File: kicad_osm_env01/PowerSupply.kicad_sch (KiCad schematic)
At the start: 79 parts

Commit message: added stml433 to schematic and carried out some mods
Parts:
- removed D1: (no value), symbol device:D_Schottky
- added R?: 1M, Resistor_SMD:R_0603_1608Metric, symbol OSM_env01-rescue:R-ESP32-EVB_Rev_D
- BAT1: value (none) -> 18650; footprint (none) -> Devtank_PCB_lib:BatteryHolder_Keystone_1042_1x18650
- C10: value (none) -> 4.7nF; footprint (none) -> Capacitor_SMD:C_0402_1005Metric
- C11, C3, C4, C9: value (none) -> 47uF; footprint (none) -> Capacitor_SMD:C_0805_2012Metric
- C14, C25, C63, C8: value (none) -> 1uF; footprint (none) -> Capacitor_SMD:C_0402_1005Metric
- C2, C24, C5: value (none) -> 10uF; footprint (none) -> Capacitor_SMD:C_0603_1608Metric
- C22, C23: value (none) -> 100nF; footprint (none) -> Capacitor_SMD:C_0402_1005Metric
- C31, C6, C7: value (none) -> DNF; footprint (none) -> Capacitor_SMD:C_0603_1608Metric
- C32, C72: value (none) -> DNF; footprint (none) -> Capacitor_SMD:C_0402_1005Metric
- C46: value (none) -> DNF; footprint (none) -> Capacitor_SMD:CP_Elec_4x5.4
- D10: value (none) -> DNF; footprint (none) -> Diode_SMD:D_SOD-123
- D11, D15: value (none) -> RED; footprint (none) -> LED_SMD:LED_0603_1608Metric
- D13: value (none) -> GRN; footprint (none) -> Devtank_PCB_lib:LED_Rectangular_W4.5mm_H7.3mm_Horizontal_2.54mm_Z3.0mm
- D14: value (none) -> YLW; footprint (none) -> Devtank_PCB_lib:LED_Rectangular_W4.5mm_H7.3mm_Horizontal_2.54mm_Z3.0mm
- D2, D3, D4, D9: value (none) -> RB160M-40TR; footprint (none) -> Diode_SMD:D_SOD-123
- D5: value (none) -> SMFE5-0A; footprint (none) -> Diode_SMD:D_SOD-123
- L1: value (none) -> 10uH; footprint (none) -> Inductor_SMD:L_1812_4532Metric
- Q1: value (none) -> SI2301BDS-T1-E3; footprint (none) -> Package_TO_SOT_SMD:SOT-23
- Q4: value (none) -> IRF7509TRPBF; footprint (none) -> Package_SO:SO-8_3.9x4.9mm_P1.27mm
- R127, R27, R54: value (none) -> DNF; footprint (none) -> Resistor_SMD:R_0603_1608Metric
- R128, R20, R28, R32, R52: value (none) -> 0R; footprint (none) -> Resistor_SMD:R_0603_1608Metric
- R18, R21, R58: value (none) -> 1M; footprint (none) -> Resistor_SMD:R_0603_1608Metric
- R19, R22, R64: value (none) -> 470k; footprint (none) -> Resistor_SMD:R_0603_1608Metric
- R41, R53: value (none) -> 2.2k; footprint (none) -> Resistor_SMD:R_0603_1608Metric
- R42, R44: value (none) -> 1.6k; footprint (none) -> Resistor_SMD:R_0603_1608Metric
- R43, R45: value (none) -> 4.99k; footprint (none) -> Resistor_SMD:R_0603_1608Metric
- R46: value (none) -> 110k; footprint (none) -> Resistor_SMD:R_0603_1608Metric
- R47: value (none) -> 36k; footprint (none) -> Resistor_SMD:R_0603_1608Metric
- R56: value (none) -> 10k; footprint (none) -> Resistor_SMD:R_0603_1608Metric
- R57, R68, R69: value (none) -> 100k; footprint (none) -> Resistor_SMD:R_0603_1608Metric
- R59, R60, R61, R62: value (none) -> 0R; footprint (none) -> Resistor_SMD:R_0805_2012Metric
- R67: value (none) -> 300k; footprint (none) -> Resistor_SMD:R_0603_1608Metric
- SW3: value (none) -> SW_Push; footprint (none) -> Devtank_PCB_lib:SW_Tactile_SPST_Angled_PTS645Vx58-2LFS
- TH2: value (none) -> 10K; footprint (none) -> Resistor_SMD:R_1206_3216Metric
- TP18, TP27, TP29, TP79: value (none) -> Test_Point; footprint (none) -> TestPoint:TestPoint_Pad_D1.5mm
- TP19, TP26: renamed from TP?; value (none) -> Test_Point; footprint (none) -> TestPoint:TestPoint_THTPad_D1.0mm_Drill0.5mm
- TP25: value (none) -> Test_Point; footprint (none) -> TestPoint:TestPoint_THTPad_D1.0mm_Drill0.5mm
- TP28: renamed from TP?; value (none) -> Test_Point; footprint (none) -> TestPoint:TestPoint_Pad_D1.5mm
- U1: value (none) -> MIC2250-1YD5; footprint (none) -> Package_TO_SOT_SMD:SOT-23-5
- U2: value (none) -> MCP73833; footprint (none) -> Package_SO:MSOP-10_3x3mm_P0.5mm
- U4: value (none) -> MIC5219-3.3; footprint (none) -> Package_TO_SOT_SMD:SOT-23-5
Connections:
- net 5Vin: now also C3.1, C4.1, D11.2 (A), D13.2 (A), D14.2 (A), D15.2 (A), D3.2 (A), D5.1 (A1), Q1.1 (G), U2.1 (VDD1), U2.2 (VDD2)
- net BAT_OP: now also R?.2
- net GND: now also R?.1
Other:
- moved on the sheet: TP79

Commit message: updated mod list
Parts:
- added Q?: 2N7002, TO_SOT_Packages_SMD:SOT-23, symbol Transistor:2N7002
- added R? (x2): DNF, Resistor_SMD:R_0603_1608Metric, symbol OSM_env01-rescue:R-ESP32-EVB_Rev_D
- added R?: 10k, symbol device:R
- added R?: 470R, symbol device:R
- added U?: MCP73831-2-OT, TO_SOT_Packages_SMD:SOT-23-5, symbol Battery_Management:MCP73831-2-OT
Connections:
- net 5Vin: now also R?.1
- net BOOST_EN: now also Q?.3 (D)
- net GND: now also Q?.2 (S), R?.2, R?.2
- net at R53.2, U2.7 (#PG(#TE)): now also R?.1, R?.2
- net BAT_OP renamed +VBAT
- new net: Q?.1 (G), R?.1, R?.2
- new net standby_ctrl: R?.1
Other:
- note added: "Timer pin 7 available on 34 version only DNF led and resistor pull low to enable timer and pull high to disable timer applying high logic to prog prin disables device"

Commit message: updated schematics
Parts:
- removed U?: MCP73831-2-OT, TO_SOT_Packages_SMD:SOT-23-5, symbol Battery_Management:MCP73831-2-OT
- added C? (x2): DNF, symbol device:C
- added C? (x2): 100nF, Capacitor_SMD:C_0603_1608Metric, symbol device:C_Small
- added D?: BZX84C10, Package_TO_SOT_SMD:SOT-23, symbol precharge-rescue:BZX84-C10,215
- added F?: 1206L050/15YR, Fuse:Fuse_1206_3216Metric, symbol precharge-rescue:Polyfuse-Device
- added Q?: SIRA01DP, hw-precharge-controller:SIRA01DP-T1-GE3, symbol precharge:SIRA01DP
- added R?: 470R, Resistor_SMD:R_0805_2012Metric, symbol device:R_Small
- added U?: MCP73832T-2ACI/MC, TO_SOT_Packages_SMD:SOT-23-5, symbol Devtank:MCP73832T-2AC
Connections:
- net 5Vin: now also C?.1, U?.1 (VDD), U?.2 (VDD)
- net BATV: now also C?.1, F?.2, U?.3 (VBAT), U?.4 (VBAT); no longer Q1.3 (D), R54.1, TP18.1
- net GND: now also C?.2, C?.2, C?.2, R?.2, U?.6 (VSS)
- net STAT1: now also U?.5 (STAT)
- net RPROG: now reaches R43.1, R45.1, U2.6 (PROG)
- net RPROG: now also U?.8 (PROG)
- new net: C?.1, D?.3 (K), Q1.3 (D), Q?.1 (S), Q?.2 (S), Q?.3 (S), R54.1, TP18.1
- new net: C?.1, F?.1, Q?.5 (D), Q?.6 (D), Q?.7 (D), Q?.8 (D)
- new net: C?.2, D?.1 (A), Q?.4 (G), R?.1
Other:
- note added: "Battery switch to power stm"
- note added: "Dual footprint battery charge controller"
- note added: "Fit capacitors as 4.7uF if used"
- note added: "Li_Ion Battery Charge Controller with reverse polarity protection"
- note added: "Note: when mcp73834 fitted: Timer pin 7 available on 34 version only DNF led and resistor pull low to enable timer and pull high to disable timer applying high logic to prog prin disables device"
- note added: "Reverse polarity protection"
- note removed: "Li_Ion Battery Charge Controller"
- note removed: "Timer pin 7 available on 34 version only DNF led and resistor pull low to enable timer and pull high to disable timer applying high logic to prog prin disables device"
- moved on the sheet: BAT1, C10, C11, C14, C2, C22, C23, C24, C25, C3, C31, C32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

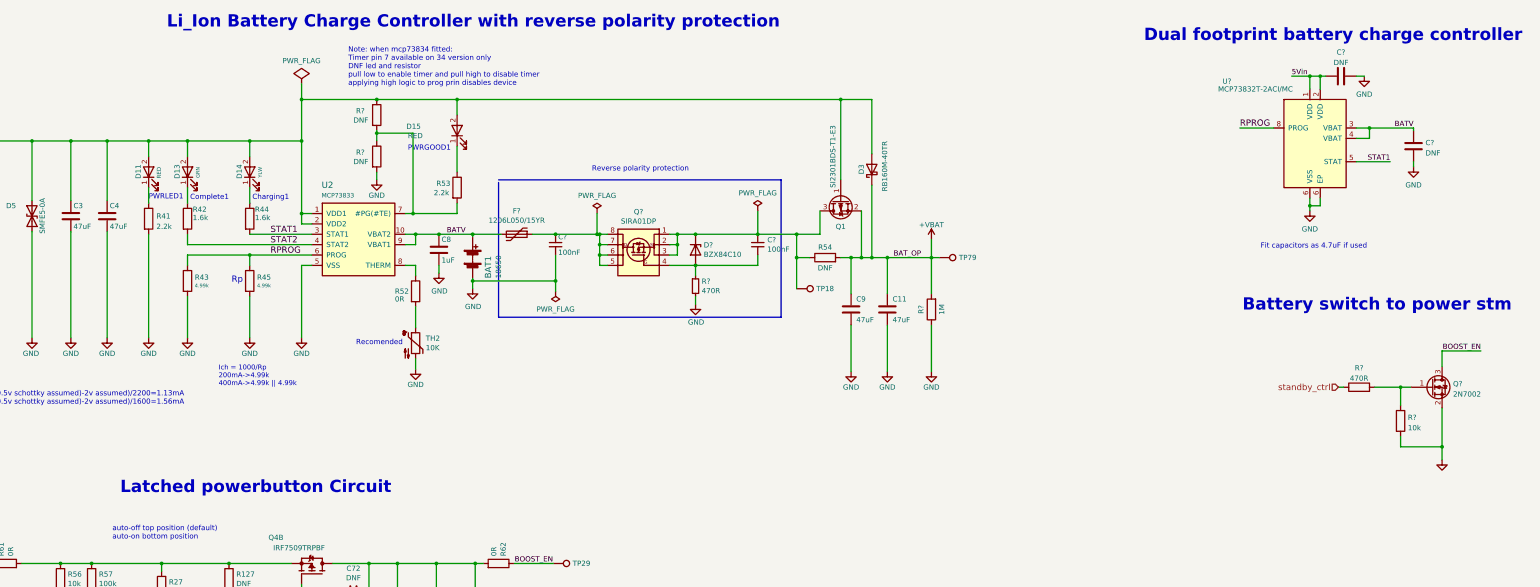
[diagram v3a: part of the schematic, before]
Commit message: added new battery charge ic u2
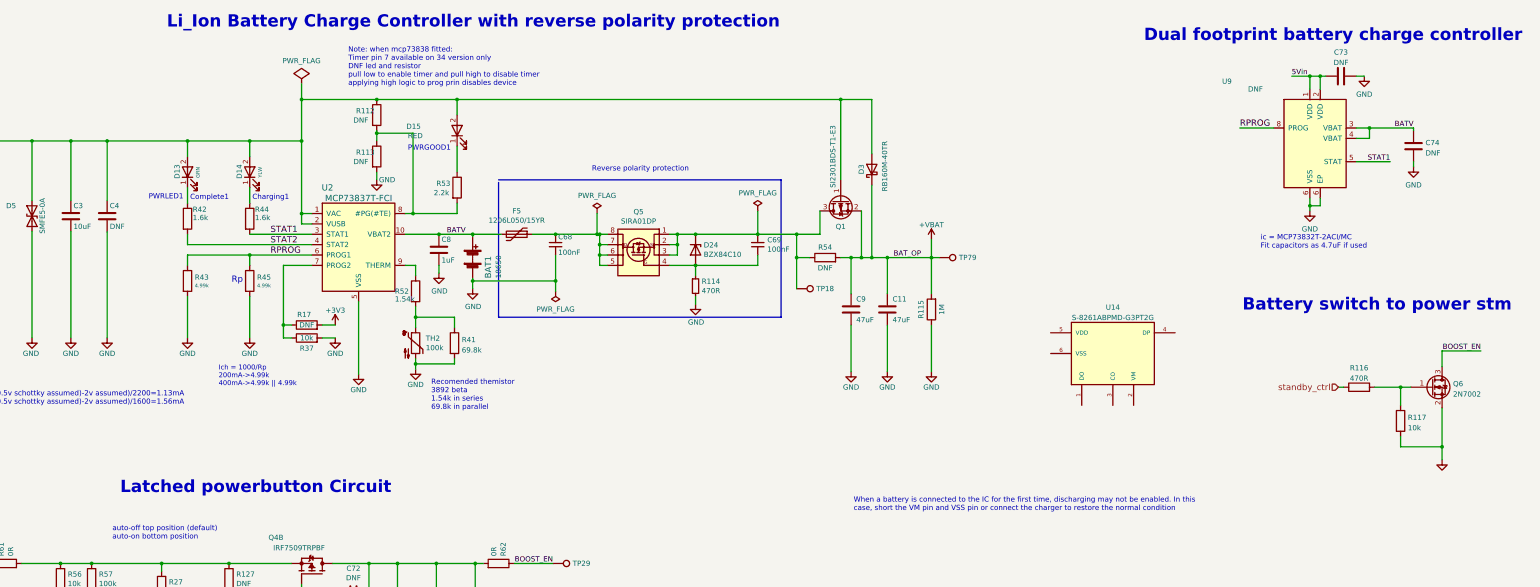
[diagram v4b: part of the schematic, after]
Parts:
- removed D11: RED, LED_SMD:LED_0603_1608Metric, symbol device:LED
- removed R41: 2.2k, Resistor_SMD:R_0603_1608Metric, symbol OSM_env01-rescue:R-ESP32-EVB_Rev_D
- removed U2: MCP73833, Package_SO:MSOP-10_3x3mm_P0.5mm, symbol OSM_env01-rescue:MCP73833(MSOP10)-ESP32-EVB_Rev_D
- added R17: 10k, symbol device:R
- added R37: DNF, symbol device:R
- added R41: 69.8k, symbol device:R
- added U14: S-8261ABPMD-G3PT2G, symbol Devtank:S-8261ABPMD-G3PT2G
- added U2: MCP73837T-FCI, symbol Devtank:MCP73837T-FCI
- C3: value 47uF -> 10uF
- C4: value 47uF -> DNF
- R52: value 0R -> 1.54k
- TH2: value 10K -> 100k
- U9: renamed from U?; value MCP73832T-2ACI/MC -> DNF
- gave numbers to parts that had none: 14
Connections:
- net +3V3: now also R17.2
- net 5Vin: now also U2.1 (VAC), U2.2 (VUSB)
- net BATV: now also U2.10 (VBAT2)
- net GND: now also R37.2, R41.2, U2.5 (VSS)
- net RPROG: now also U2.6 (PROG1)
- net STAT1: now also U2.3 (STAT1)
- net STAT2: now also U2.4 (STAT2)
- net at R52.1: now also U2.9 (THERM)
- net at R52.2, TH2.1: now also R41.1
- net at R112.2, R113.1, R53.2: now also U2.8 (#PG(#TE))
- new net: R17.1, R37.1, U2.7 (PROG2)
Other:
- note added: "Note: when mcp73838 fitted: Timer pin 7 available on 34 version only DNF led and resistor pull low to enable timer and pull high to disable timer applying high logic to prog prin disables device"
- note added: "Recomended themistor 3892 beta 1.54k in series 69.8k in parallel"
- note added: "When a battery is connected to the IC for the first time, discharging may not be enabled. In this case, short the VM pin and VSS pin or connect the charger to restore the normal condition"
- note added: "ic = MCP73832T-2ACI/MC Fit capacitors as 4.7uF if used"
- note removed: "Fit capacitors as 4.7uF if used"
- note removed: "Note: when mcp73834 fitted: Timer pin 7 available on 34 version only DNF led and resistor pull low to enable timer and pull high to disable timer applying high logic to prog prin disables device"
- note removed: "Recomended"

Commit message: updated schematics and added rs232
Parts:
- added C65: 100nF, symbol Device:C
- added Q7: FDS9926A, Package_SO:SOIC-8_3.9x4.9mm_P1.27mm, symbol Transistor_FET:FDS9926A
- added R102: 2k, symbol Device:R
- added R98: 470R, symbol Device:R
- added TP65: TestPoint, symbol Connector:TestPoint
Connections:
- net 5Vin: no longer D3.2 (A), Q1.1 (G)
- net GND: now also Q7.1 (S1), R102.2
- net at C69.1, D24.3 (K), Q5.1 (S)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: now also R98.1; no longer Q1.3 (D), R54.1, TP18.1
- net at U14.1 (DO): now also Q7.4 (G2)
- net at U14.2 (VM): now also R102.1
- net at U14.3 (CO): now also Q7.2 (G1)
- net at U14.4 (DP): now also TP65.1
- net at U14.5 (VDD): now also C65.1, R98.2
- net at U14.6 (VSS): now also C65.2, Q7.3 (S2)
- net +VBAT renamed BAT_OP
- new net: Q1.3 (D), R54.1, TP18.1
- new net: D3.2 (A), Q1.1 (G)
- new net: Q7.5 (D2), Q7.6 (D2), Q7.7 (D1), Q7.8 (D1)
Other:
- note added: "check footprint 7and8 connected. 5 and 6 connected together."
- moved on the sheet: BAT1, C11, C68, C69, C73, C74, C9, D24, D3, F5, Q1, Q5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

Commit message: Schematics waiting review
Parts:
- removed C14: 1uF, Capacitor_SMD:C_0402_1005Metric, symbol OSM_env01-rescue:C-device-ESP32-EVB_Rev_D-rescue
- removed C22, C23: 100nF, Capacitor_SMD:C_0402_1005Metric, symbol OSM_env01-rescue:C-device-ESP32-EVB_Rev_D-rescue
- removed C24: 10uF, Capacitor_SMD:C_0603_1608Metric, symbol OSM_env01-rescue:C-device-ESP32-EVB_Rev_D-rescue
- removed C31: DNF, Capacitor_SMD:C_0603_1608Metric, symbol device:C
- removed C4: DNF, Capacitor_SMD:C_0805_2012Metric, symbol device:C
- removed C68, C69: 100nF, Capacitor_SMD:C_0603_1608Metric, symbol device:C_Small
- removed C72: DNF, Capacitor_SMD:C_0402_1005Metric, symbol device:C
- removed C73: DNF, symbol device:C
- removed C8: 1uF, Capacitor_SMD:C_0402_1005Metric, symbol device:C
- removed D10: DNF, Diode_SMD:D_SOD-123, symbol device:D
- removed D13: GRN, Devtank_PCB_lib:LED_Rectangular_W4.5mm_H7.3mm_Horizontal_2.54mm_Z3.0mm, symbol device:LED
- removed D15: RED, LED_SMD:LED_0603_1608Metric, symbol device:LED
- removed D24: BZX84C10, Package_TO_SOT_SMD:SOT-23, symbol precharge-rescue:BZX84-C10,215
- removed D4: RB160M-40TR, Diode_SMD:D_SOD-123, symbol OSM_env01-rescue:D_Schottky-device-ESP32-EVB_Rev_D-rescue
- removed F5: 1206L050/15YR, Fuse:Fuse_1206_3216Metric, symbol precharge-rescue:Polyfuse-Device
- removed Q4: IRF7509TRPBF, Package_SO:SO-8_3.9x4.9mm_P1.27mm, symbol OSM_env01-rescue:IRF7319TRPBF-Devtank-ESP32-EVB_Rev_D-rescue
- removed Q5: SIRA01DP, hw-precharge-controller:SIRA01DP-T1-GE3, symbol precharge:SIRA01DP
- removed Q6: 2N7002, TO_SOT_Packages_SMD:SOT-23, symbol Transistor:2N7002
- removed R112, R113: DNF, Resistor_SMD:R_0603_1608Metric, symbol OSM_env01-rescue:R-ESP32-EVB_Rev_D
- removed R114: 470R, Resistor_SMD:R_0805_2012Metric, symbol device:R_Small
- removed R115: 1M, Resistor_SMD:R_0603_1608Metric, symbol OSM_env01-rescue:R-ESP32-EVB_Rev_D
- removed R117, R17: 10k, symbol device:R
- removed R127, R27: DNF, Resistor_SMD:R_0603_1608Metric, symbol device:R
- removed R21: 1M, Resistor_SMD:R_0603_1608Metric, symbol device:R
- removed R22: 470k, Resistor_SMD:R_0603_1608Metric, symbol device:R
- removed R28, R32: 0R, Resistor_SMD:R_0603_1608Metric, symbol device:R
- removed R37: DNF, symbol device:R
- removed R41: 69.8k, symbol device:R
- removed R42: 1.6k, Resistor_SMD:R_0603_1608Metric, symbol OSM_env01-rescue:R-ESP32-EVB_Rev_D
- removed R43, R45: 4.99k, Resistor_SMD:R_0603_1608Metric, symbol OSM_env01-rescue:R-ESP32-EVB_Rev_D
- removed R52: 1.54k, Resistor_SMD:R_0603_1608Metric, symbol OSM_env01-rescue:R-ESP32-EVB_Rev_D
- removed R53: 2.2k, Resistor_SMD:R_0603_1608Metric, symbol OSM_env01-rescue:R-ESP32-EVB_Rev_D
- removed R56: 10k, Resistor_SMD:R_0603_1608Metric, symbol OSM_env01-rescue:R-device-ESP32-EVB_Rev_D-rescue
- removed R57, R68, R69: 100k, Resistor_SMD:R_0603_1608Metric, symbol OSM_env01-rescue:R-device-ESP32-EVB_Rev_D-rescue
- removed R61, R62: 0R, Resistor_SMD:R_0805_2012Metric, symbol device:R
- removed R67: 300k, Resistor_SMD:R_0603_1608Metric, symbol OSM_env01-rescue:R-device-ESP32-EVB_Rev_D-rescue
- removed SW3: SW_Push, Devtank_PCB_lib:SW_Tactile_SPST_Angled_PTS645Vx58-2LFS, symbol Switch:SW_Push
- removed TH2: 100k, Resistor_SMD:R_1206_3216Metric, symbol OSM_env01-rescue:Thermistor_NTC-device-ESP32-EVB_Rev_D-rescue
- removed TP19: Test_Point, TestPoint:TestPoint_THTPad_D1.0mm_Drill0.5mm, symbol OSM_env01-rescue:Test_Point-Connector-ESP32-EVB_Rev_D-rescue
- removed TP27, TP28, TP29: Test_Point, TestPoint:TestPoint_Pad_D1.5mm, symbol OSM_env01-rescue:Test_Point-Connector-ESP32-EVB_Rev_D-rescue
- removed U1: MIC2250-1YD5, Package_TO_SOT_SMD:SOT-23-5, symbol OSM_env01-rescue:MIC2288YD5-TR_BOOST-Devtank-ESP32-EVB_Rev_D-rescue
- removed U2: MCP73837T-FCI, symbol Devtank:MCP73837T-FCI
- removed U4: MIC5219-3.3, Package_TO_SOT_SMD:SOT-23-5, symbol regul:MIC5219-3.3
- removed U9: DNF, TO_SOT_Packages_SMD:SOT-23-5, symbol Devtank:MCP73832T-2AC
- added C14: DNF, Capacitor_SMD:C_0402_1005Metric, symbol device:C
- added C22: 1uF, Capacitor_SMD:C_0402_1005Metric, symbol device:C
- added C24: DNF, Capacitor_SMD:CP_Elec_4x5.4, symbol device:C
- added C31: DNF, Capacitor_SMD:C_0603_1608Metric, symbol OSM_env01-rescue:C-device-ESP32-EVB_Rev_D-rescue
- added C33: DNF, Capacitor_SMD:C_0805_2012Metric, symbol device:C
- added C34: DNF, symbol Device:C
- added D10: RB160M-40TR, Diode_SMD:D_SOD-123, symbol OSM_env01-rescue:D_Schottky-device-ESP32-EVB_Rev_D-rescue
- added JP19: Jumper_2_Open, symbol Jumper:Jumper_2_Open
- added R112, R114: 1M, Resistor_SMD:R_0603_1608Metric, symbol device:R
- added R113: 470k, Resistor_SMD:R_0603_1608Metric, symbol device:R
- added R115, R68: 0R, Resistor_SMD:R_0603_1608Metric, symbol device:R
- added R131: 10k, Resistor_SMD:R_0603_1608Metric, symbol device:R
- added R45, R69: 0R, symbol Device:R
- added R5: (no value), symbol Device:R
- added R52: 5k, symbol device:R
- added R70: 0R, Resistor_SMD:R_0805_2012Metric, symbol device:R
- added SW1: EG1247, symbol Switch:SW_SPDT
- added TH1: 10k, symbol device:Thermistor
- added TP34, TP77: Test_Point, TestPoint:TestPoint_Pad_D1.5mm, symbol OSM_env01-rescue:Test_Point-Connector-ESP32-EVB_Rev_D-rescue
- added TP52: Test_Point, TestPoint:TestPoint_THTPad_D1.0mm_Drill0.5mm, symbol OSM_env01-rescue:Test_Point-Connector-ESP32-EVB_Rev_D-rescue
- added U1: MIC2251YML-TR, MLF-8_ML_MCH, symbol Devtank:MIC2251YML-TR
- added U17: MIC5219-3.3YMM, Package_SO:MSOP-8_3x3mm_P0.65mm, symbol Regulator_Linear:MIC5219-3.3YMM
- added U2: MCP73832T-2AC, TO_SOT_Packages_SMD:SOT-23-5, symbol Devtank:MCP73832T-2AC
- added U4: MIC5219-3.3YMM, symbol Regulator_Linear:MIC5219-3.3YMM
- added U9: DNF, Package_TO_SOT_SMD:SOT-23-5, symbol Battery_Management:MCP73832-2-OT
- C11: value 47uF -> DNF; footprint Capacitor_SMD:C_0805_2012Metric -> Capacitor_SMD:C_0603_1608Metric; Package 0805 -> (none)
- C3: value 10uF -> 4.7uF
- C46: symbol device:CP -> device:C
- C74: value DNF -> 4.7uF
- C9: value 47uF -> 1uF; footprint Capacitor_SMD:C_0805_2012Metric -> Capacitor_SMD:C_0402_1005Metric; Package 0805 -> (none)
- R116: value 470R -> 470k; footprint (none) -> Resistor_SMD:R_0603_1608Metric; Tolerance (none) -> 0.1%
- R128: value 0R -> DNF
- R18, R19, R58, R64: Tolerance (none) -> 0.1%
- R44: value 1.6k -> 2k
- TP65: value TestPoint -> Test_Point
- U14: value S-8261ABPMD-G3PT2G -> S-8261ACBMD-G4BT2U
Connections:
- net +5V: now also C9.1, D10.1 (K), R68.1, U17.2 (IN), U4.2 (IN)
- net 5Vin: now also D3.2 (A), Q1.1 (G), C33.1, R114.1, R45.1, R45.2, U2.1 (VDD), U2.2 (VDD), U9.4 (VDD)
- net BOOST_EN: now also D3.1 (K), Q1.2 (S), R54.2, TP79.1, C31.1, R115.1, U1.6 (VIN)
- net GND: now also R116.2, R128.2, C14.2, C22.2, C24.2, C31.2, C33.2, R113.2, R52.2, TH1.2, U1.2 (AGND), U1.3 (PGND), U1.9 (EP), U17.5 (GND), U17.6 (GND), U17.7 (GND), U17.8 (GND), U2.6 (VSS), U2.9 (EP), U4.5 (GND), U4.6 (GND), U4.7 (GND), U4.8 (GND), U9.2 (VSS); no longer BAT1.2 (-)
- net RPROG: now also R52.1, U2.8 (PROG), U9.5 (PROG)
- net STAT1: now also U2.5 (STAT), U9.1 (STAT)
- net at Q1.3 (D), R54.1: now also R5.2; no longer TP18.1
- net at D2.2 (A), L1.2: now also U1.4 (SW)
- net at R46.2, R47.1: now also U1.1 (FB)
- net at C7.1, R20.2: now also U1.8 (EN)
- net at R128.1: now also R115.2, U1.7 (DITH)
- net at C46.1, C63.1, D9.2 (A)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: now also U4.3 (OUT)
- net at C32.1: now also U4.4 (BP)
- net protection_ic_vss: now reaches C65.2, Q7.3 (S2), U14.6 (VSS)
- net protection_ic_vss: now also BAT1.2 (-), C34.2, JP19.2 (B), TP77.1
- net at R98.1: now also TP18.1, R5.1, SW1.3 (C)
- net at R102.1, U14.2 (VM): now also JP19.1 (A)
- net at C65.1, R98.2, U14.5 (VDD): now also C34.1
- net 3V3_RAIL_MON renamed 3V3_BOARD_MONITOR
- net BATV renamed BATTERY_VOLTAGE
- net BATTERY_VOLTAGE: now also SW1.2 (B), TP34.1, U2.3 (VBAT), U2.4 (VBAT), U9.3 (VBAT)
- removed net BAT_OP: C11.1, C9.1, D3.1 (K), Q1.2 (S), R54.2, TP79.1
- net BatMon renamed VBAT_MONITOR
- net standby_ctrl renamed 5V_RAIL_MONITOR
- net 5V_RAIL_MONITOR: now also R114.2
- new net: C22.1, C24.1, D10.2 (A), R70.2, U17.3 (OUT)
- new net: R69.2, U4.1 (EN)
- new net: C11.1, R68.2, U17.1 (EN)
- new net: C14.1, U17.4 (BP)
- new net +3V3_CORE: R112.1, R131.1, R70.1, TP52.1
- new net 3V3_BOARD_EN: R69.1
- new net 3V3_CORE_MONITOR: R112.2, R113.1
- new net BATT_TEMP_MONITOR: R131.2, TH1.1
- no-connect marks 0 -> 1
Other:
- note added: "3V3_BOARD"
- note added: "3V3_BOARD Monitor"
- note added: "3V3_CORE"
- note added: "3V3_CORE Monitor"
- note added: "5Vin Monitor"
- note added: "Battery Temperature Monitor"
- note added: "D14 LED resistor calculation 5-2/1.5mA=2k"
- note added: "Li_Ion Battery Charge Controller with battery protection"
- note added: "Second footprint for battery charge controller"
- note added: "To do -unsure aboiut how to implemnt tristate status output on mcp battery charge controller"
- note added: "When a battery is connected to the IC (u14) for the first time, discharging may not be enabled. In this case, short the VM pin and VSS pin or connect the charger to restore the normal condition In the case the battery charge protection ic is unavailable. All protection ic r's and c's can be removed and fit r5"
- note removed: "Battery switch to power stm"
- note removed: "Charging1"
- note removed: "Complete1"
- note removed: "Dual footprint battery charge controller"
- note removed: "Ich = 1000/Rp 200mA->4.99k 400mA->4.99k || 4.99k"
- note removed: "Latched powerbutton Circuit"
- note removed: "Led calcs d11 and d15 = ((5-0.5v schottky assumed)-2v assumed)/2200=1.13mA d11 and d15 = ((5-0.5v schottky assumed)-2v assumed)/1600=1.56mA"
- note removed: "Li_Ion Battery Charge Controller with reverse polarity protection"
- note removed: "Note: when mcp73838 fitted: Timer pin 7 available on 34 version only DNF led and resistor pull low to enable timer and pull high to disable timer applying high logic to prog prin disables device"
- note removed: "PWRGOOD1"
- note removed: "PWRLED1"
- note removed: "Recomended themistor 3892 beta 1.54k in series 69.8k in parallel"
- note removed: "Reverse polarity protection"
- note removed: "Rp"
- note removed: "Voltage Rail Monitor"
- note removed: "When a battery is connected to the IC for the first time, discharging may not be enabled. In this case, short the VM pin and VSS pin or connect the charger to restore the normal condition"
- note removed: "auto-off top position (default) auto-on bottom position"
- note removed: "check footprint 7and8 connected. 5 and 6 connected together."
- note removed: "ic = MCP73832T-2ACI/MC Fit capacitors as 4.7uF if used"
- moved on the sheet: BAT1, C10, C2, C25, C3, C32, C5, C6, C63, C65, C7, C74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

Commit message: before fixing devtank symbol issues
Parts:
- R5: value (none) -> DNF
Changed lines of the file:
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@@
     (in_bom yes) (on_board yes) (fields_autoplaced)
     (property "Reference" "R5" (id 0) (at 222.25 41.6392 90))
-    (property "Value" "" (id 1) (at 222.25 44.1761 90))
+    (property "Value" "DNF" (id 1) (at 222.25 44.1761 90))
     (property "Footprint" "" (id 2) (at 222.25 48.133 90)
       (effects (font (size 1.27 1.27)) hide)
@@
     (pin "1")
   )
-  (symbol (lib_name "PWR_FLAG_1") (lib_id "power:PWR_FLAG") (at 203.2 57.15 0) (unit 1)
+  (symbol (lib_id "power:PWR_FLAG") (at 203.2 57.15 0) (unit 1)
     (in_bom yes) (on_board yes) (fields_autoplaced)
     (property "Reference" "#FLG0104" (id 0) (at 203.2 55.245 0)
       (effects (font (size 1.27 1.27)) hide)
     )
-    (property "Value" "PWR_FLAG" (id 1) (at 203.2 53.5742 0))
+    (property "Value" "" (id 1) (at 203.2 53.5742 0))
     (property "Footprint" "" (id 2) (at 203.2 57.15 0)
       (effects (font (size 1.27 1.27)) hide)
@@
     (pin "9")
   )
-  (symbol (lib_name "PWR_FLAG_2") (lib_id "power:PWR_FLAG") (at 203.2 72.39 0) (mirror x) (unit 1)
+  (symbol (lib_id "power:PWR_FLAG") (at 203.2 72.39 0) (mirror x) (unit 1)
     (in_bom yes) (on_board yes) (fields_autoplaced)
     (property "Reference" "#FLG0114" (id 0) (at 203.2 74.295 0)
       (effects (font (size 1.27 1.27)) hide)
     )
-    (property "Value" "PWR_FLAG" (id 1) (at 203.2 76.8334 0))
+    (property "Value" "" (id 1) (at 203.2 76.8334 0))
     (property "Footprint" "" (id 2) (at 203.2 72.39 0)
       (effects (font (size 1.27 1.27)) hide)
